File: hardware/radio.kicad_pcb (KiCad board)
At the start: 4 copper layers, 65 x 56 mm, 89 parts, among them J1 JCLK, U1 G144A12, U3V3t1V8 NCP1117ST18T3G, U5V0t3V3 NCP1117ST33T3G

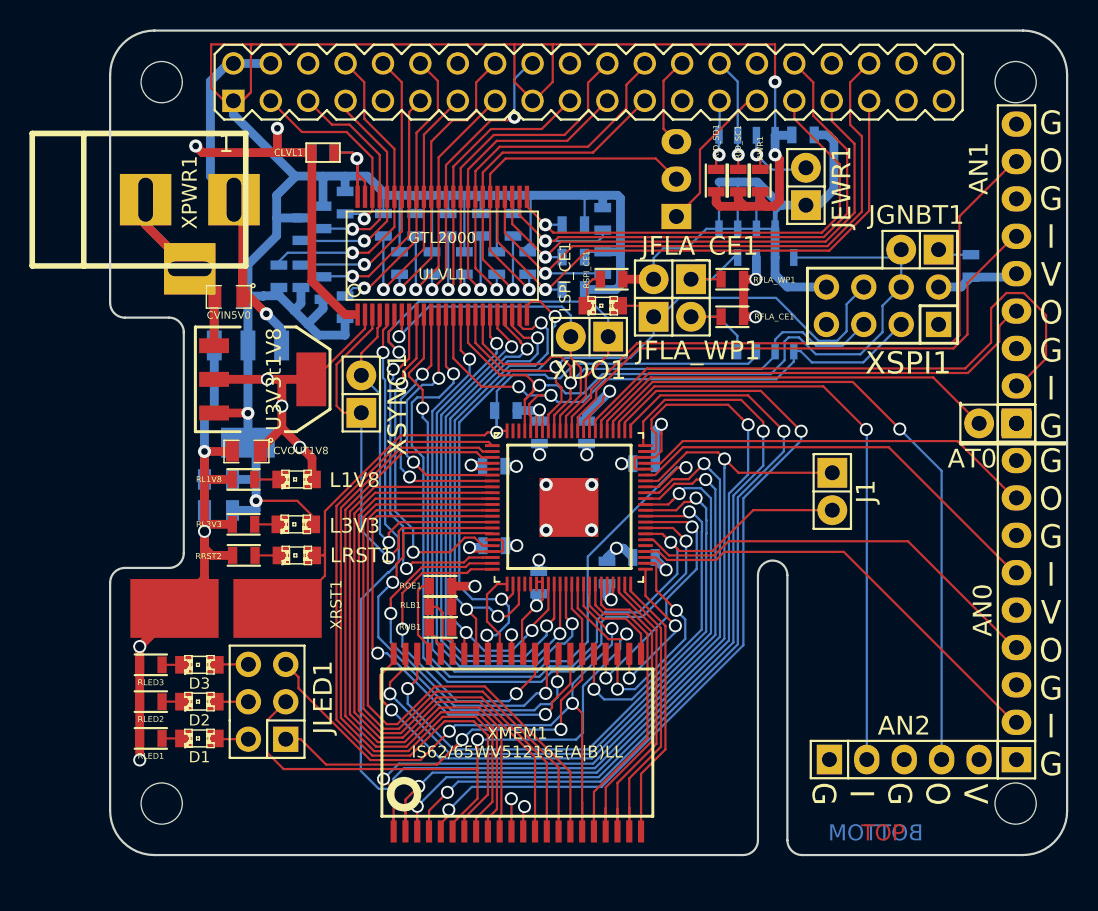
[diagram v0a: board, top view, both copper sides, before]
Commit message: Adding raspberry pi labeling.
Fixes #8.
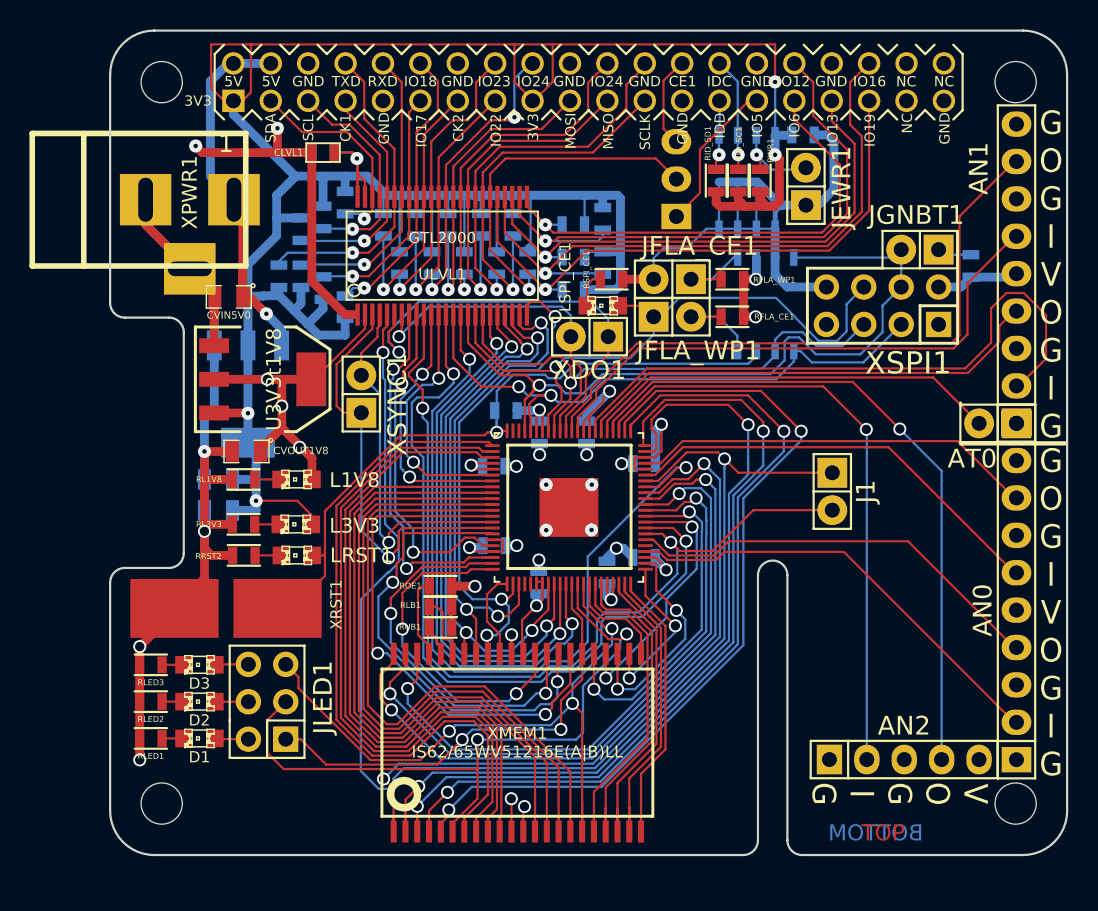
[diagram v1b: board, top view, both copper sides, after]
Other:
- net class Analog: via_drill 0.635 -> 0.3
- net class Default: via_drill 0.635 -> 0.3
- net class Memory: via_drill 0.635 -> 0.3
- net class PWR: via_drill 0.635 -> 0.3
- board text added: "3V3"
- board text added: "5V"
- board text added: "CE1"
- board text added: "CK1"
- board text added: "CK2"
- board text added: "GND"
- board text added: "IDC"
- board text added: "IDD"
- board text added: "IO12"
- board text added: "IO13"
- board text added: "IO16"
- board text added: "IO17"
- board text added: "IO18"
- board text added: "IO19"
- board text added: "IO22"
- board text added: "IO23"
- board text added: "IO24"
- board text added: "IO5"
- board text added: "IO6"
- board text added: "MISO"
- board text added: "MOSI"
- board text added: "NC"
- board text added: "RXD"
- board text added: "SCL"
- board text added: "SCLK"
- board text added: "SDA"
- board text added: "TXD"

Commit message: Fixing silkscreen issues.
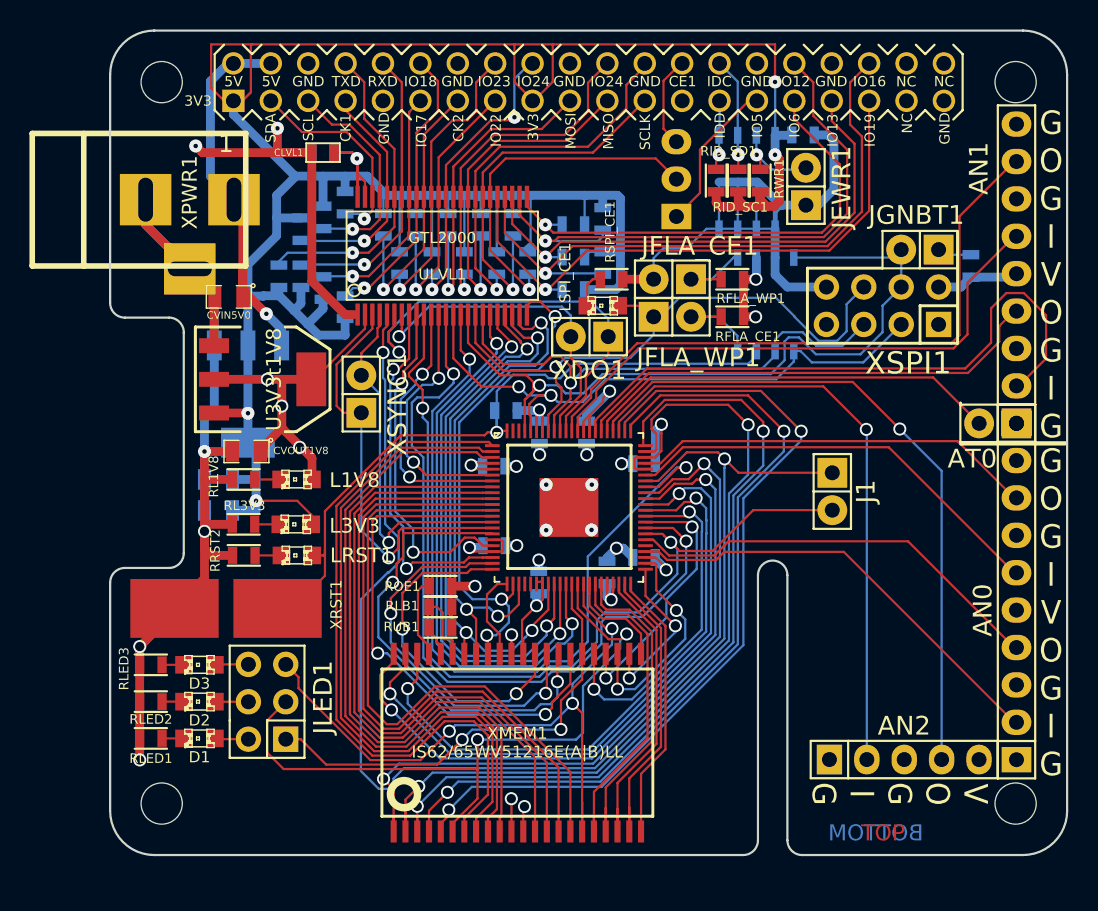
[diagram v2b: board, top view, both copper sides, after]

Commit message: Adding more stuff to silk screen.
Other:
- board text added: "Serial No"
- board text added: "Version: v0.0.0-72-g4a78914"
- board text added: "github.com/hedj/radio"
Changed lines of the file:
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@@
     (area 11.306479 15.7 93.2 83.514983)
     (thickness 1.6)
-    (drawings 154)
+    (drawings 157)
     (tracks 1840)
     (zones 0)
@@
     (descr "Through hole pin header")
     (tags "pin header")
-    (fp_text reference J1 (at 0 -2.286 270) (layer F.SilkS)
+    (fp_text reference J1 (at -0.254 2.4384 270) (layer F.SilkS)
       (effects (font (size 1.27 1.27) (thickness 0.2032)))
     )
@@
     (descr "Through hole pin header")
     (tags "pin header")
-    (fp_text reference XDO1 (at 0 -2.286 180) (layer F.SilkS)
+    (fp_text reference XDO1 (at -0.03 -2.4892 180) (layer F.SilkS)
       (effects (font (size 1.27 1.27) (thickness 0.2032)))
     )
@@
     (pad " " smd rect (at 0.5969 -0.5969) (size 0.7493 0.7493) (layers F.Paste))
   )
+  (gr_text "Version: v0.0.0-72-g4a78914" (at 58.8264 60.8076 90) (layer F.SilkS)
+    (effects (font (size 0.75 0.75) (thickness 0.1875)))
+  )
+  (gr_text "Serial No" (at 66.9036 58.2168 90) (layer F.SilkS)
+    (effects (font (size 1.5 1.5) (thickness 0.3)))
+  )
+  (gr_text github.com/hedj/radio (at 56.2864 56.7436 90) (layer F.SilkS)
+    (effects (font (size 1.5 1.5) (thickness 0.3)))
+  )
   (gr_text IO13 (at 66.02 24.09 90) (layer F.SilkS)
     (effects (font (size 0.7 0.7) (thickness 0.16)))
@@
       )
     )
+  )
+  (zone (net 0) (net_name "") (layer F.SilkS) (hatch edge 0.508)
+    (connect_pads (clearance 0.3048))
+    (min_thickness 0.254)
+    (fill yes (arc_segments 16) (thermal_gap 0.508) (thermal_bridge_width 0.508))
+    (polygon
+      (pts
+        (xy 73.3552 61.976) (xy 68.2752 61.976) (xy 68.2752 42.5704) (xy 73.3552 42.5704)
+      )
+    )

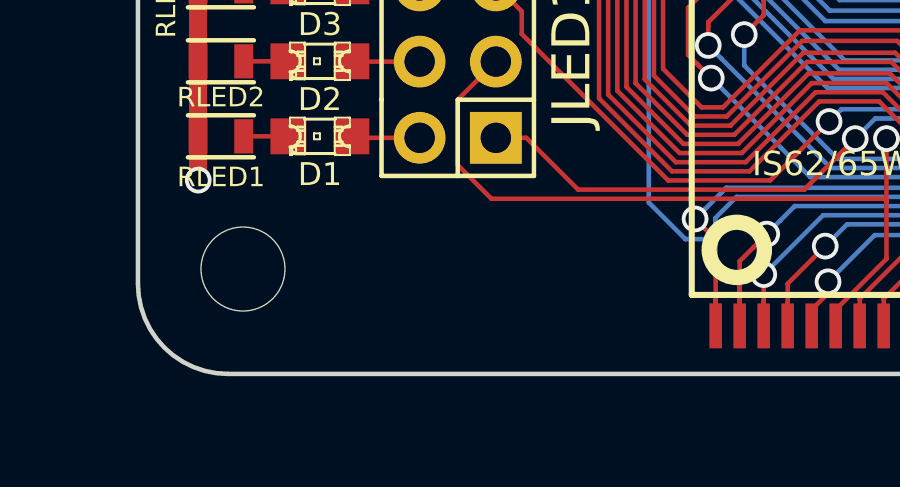
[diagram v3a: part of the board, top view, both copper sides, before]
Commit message: Adding GND connection point for testing.
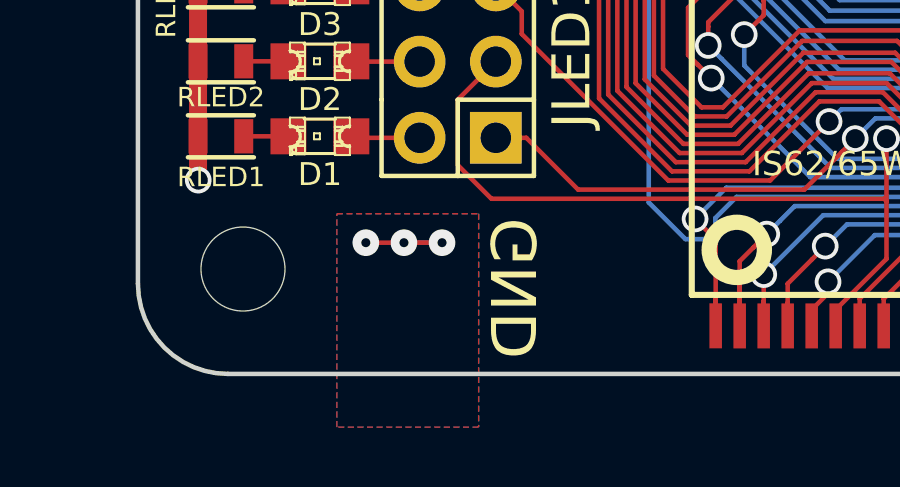
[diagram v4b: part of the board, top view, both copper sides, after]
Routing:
- net (no net): track 0.00 -> 3.81 mm, vias 0 -> 3
- added copper zone on B.Cu, net GND
- added copper zone on F.Cu, net GND
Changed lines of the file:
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@@
     (area 11.306479 15.7 93.2 83.514983)
     (thickness 1.6)
-    (drawings 157)
-    (tracks 1840)
+    (drawings 159)
+    (tracks 1845)
     (zones 0)
     (modules 89)
@@
   (page A4)
   (layers
-    (0 Top signal hide)
+    (0 Top signal)
     (1 In1.Cu power hide)
     (2 In2.Cu power hide)
-    (31 Bottom signal hide)
+    (31 Bottom signal)
     (32 B.Adhes user hide)
     (33 F.Adhes user hide)
     (34 B.Paste user hide)
     (35 F.Paste user hide)
-    (36 B.SilkS user hide)
+    (36 B.SilkS user)
     (37 F.SilkS user)
     (38 B.Mask user hide)
@@
     (user_trace_width 0.6)
     (trace_clearance 0.1524)
-    (zone_clearance 0.3048)
+    (zone_clearance 0.508)
     (zone_45_only no)
     (trace_min 0.1524)
@@
     (pad " " smd rect (at 0.5969 -0.5969) (size 0.7493 0.7493) (layers F.Paste))
   )
+  (gr_text GND (at 29.5148 70.4596 90) (layer B.SilkS)
+    (effects (font (size 1.5 1.5) (thickness 0.3)) (justify mirror))
+  )
+  (gr_text GND (at 29.5148 70.4596 90) (layer F.SilkS)
+    (effects (font (size 1.5 1.5) (thickness 0.3)) (justify mirror))
+  )
   (gr_text "Version: v0.0.0-72-g4a78914" (at 58.8264 60.8076 90) (layer F.SilkS)
     (effects (font (size 0.75 0.75) (thickness 0.1875)))
@@
   (gr_line (start 60.94 54.31) (end 60.94 72.31) (layer Edge.Cuts) (width 0.15))
   (gr_line (start 62.94 54.31) (end 62.94 72.31) (layer Edge.Cuts) (width 0.15))
+  (via (at 25.8064 68.9356) (size 0.889) (layers Top Bottom) (net 0))
+  (via (at 24.5364 68.9356) (size 0.889) (layers Top Bottom) (net 0))
+  (segment (start 24.5364 68.9356) (end 27.0764 68.9356) (width 0.1524) (layer Top) (net 0))
+  (via (at 27.0764 68.9356) (size 0.889) (layers Top Bottom) (net 0))
+  (segment (start 27.0764 68.9356) (end 25.8064 68.9356) (width 0.1524) (layer Bottom) (net 0))
   (segment (start 44.207256 58.818753) (end 44.207256 58.350869) (width 0.1524) (layer Top) (net 1))
   (via (at 44.207256 58.350869) (size 0.889) (drill 0.635) (layers Top Bottom) (net 1))
@@
       )
     )
+  )
+  (zone (net 1) (net_name GND) (layer Top) (hatch edge 0.508)
+    (connect_pads (clearance 0.508))
+    (min_thickness 0.254)
+    (fill (arc_segments 16) (thermal_gap 0.508) (thermal_bridge_width 0.508))
+    (polygon
+      (pts
+        (xy 28.2956 75.0824) (xy 23.5712 75.0824) (xy 23.5712 67.9704) (xy 28.2956 67.9704)
+      )
+    )
+  )
+  (zone (net 1) (net_name GND) (layer Bottom) (hatch edge 0.508)
+    (connect_pads (clearance 0.508))
+    (min_thickness 0.254)
+    (fill (arc_segments 16) (thermal_gap 0.508) (thermal_bridge_width 0.508))
+    (polygon
+      (pts
+        (xy 28.2956 75.0824) (xy 23.5712 75.0824) (xy 23.5712 67.9704) (xy 28.2956 67.9704)
+      )
+    )

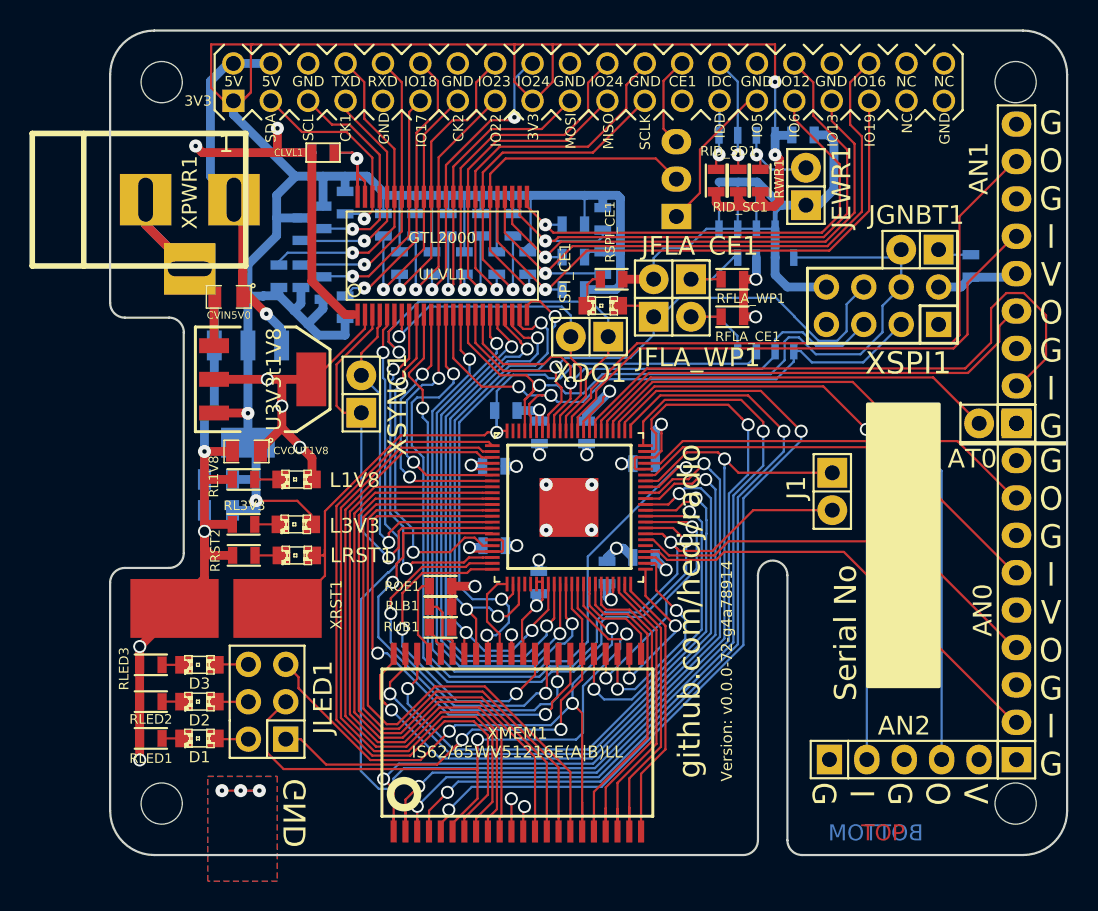
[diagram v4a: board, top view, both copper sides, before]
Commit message: More silkscreen updates.
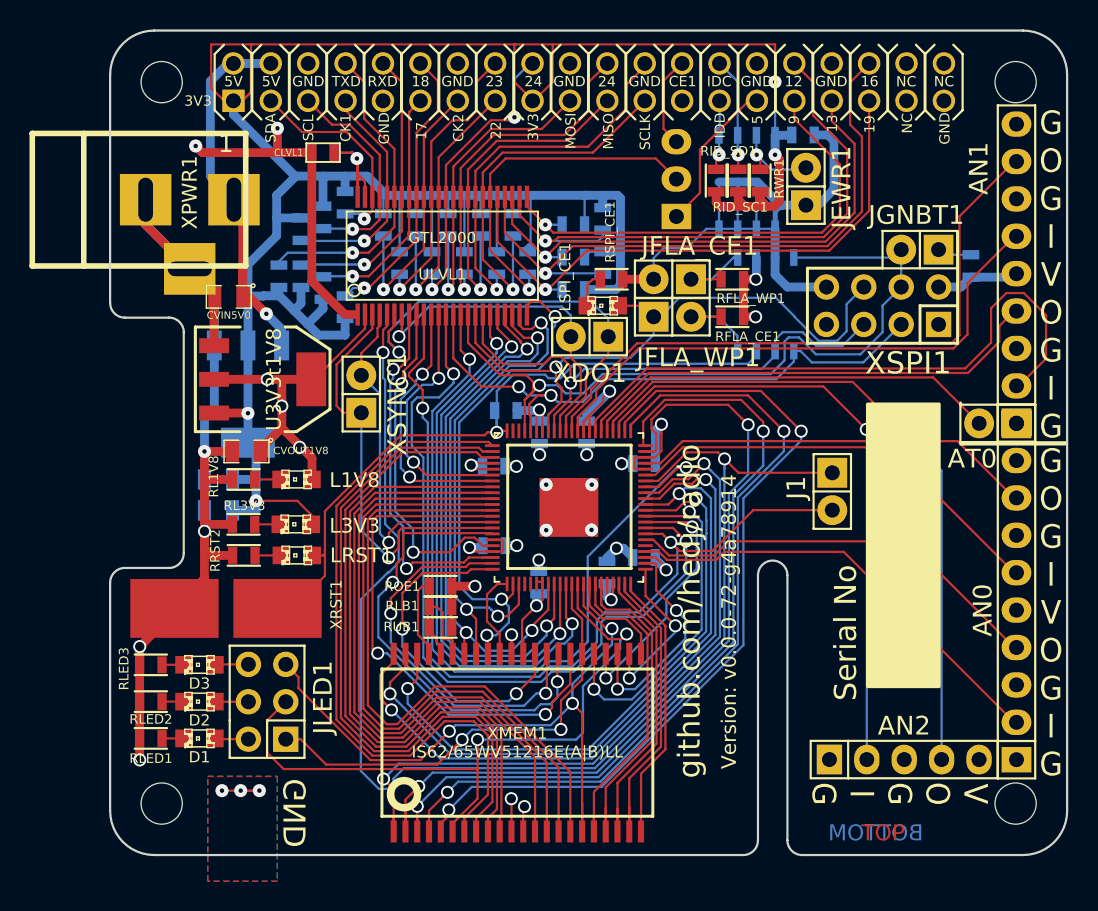
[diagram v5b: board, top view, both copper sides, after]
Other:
- board text added: "12"
- board text added: "13"
- board text added: "16"
- board text added: "17"
- board text added: "18"
- board text added: "19"
- board text added: "22"
- board text added: "23"
- board text added: "24"
- board text added: "5"
- board text added: "6"
- board text removed: "IO12"
- board text removed: "IO13"
- board text removed: "IO16"
- board text removed: "IO17"
- board text removed: "IO18"
- board text removed: "IO19"
- board text removed: "IO22"
- board text removed: "IO23"
- board text removed: "IO24"
- board text removed: "IO5"
- board text removed: "IO6"

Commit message: Adding openhardware logo.
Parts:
- added G***: LOGO, logo:OSHWLOGO0.3IN, B.Cu at (65.0, 58.9)
